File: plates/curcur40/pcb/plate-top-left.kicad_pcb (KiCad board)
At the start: 2 copper layers, 125.1 x 92.6 mm, 0 parts

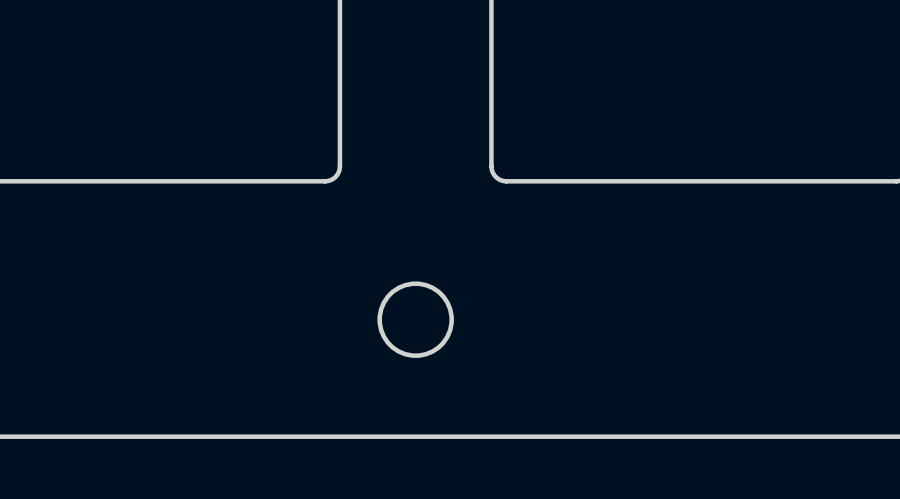
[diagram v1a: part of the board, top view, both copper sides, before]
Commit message: feat(mech): align left thumb mounting hole L5 (-21.5250, 63.6875) symmetrically with right TB4
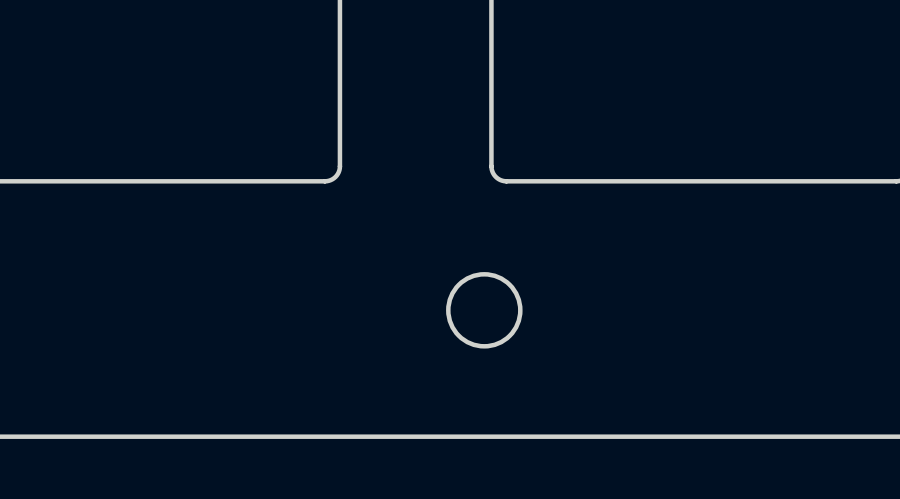
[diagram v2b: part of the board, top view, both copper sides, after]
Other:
- outline, holes or cut-outs redrawn
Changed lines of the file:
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@@
 	)
 	(gr_circle
-		(center -23.8125 64)
-		(end -22.6125 64)
+		(center -21.525 63.6875)
+		(end -20.325 63.6875)
 		(stroke
 			(width 0.15)
